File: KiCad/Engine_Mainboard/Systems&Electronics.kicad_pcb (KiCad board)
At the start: 2 copper layers, 182.4 x 143.2 mm, 54 parts, among them J1 Pressure Transducer, J12 Screw_Terminal_01x02, J13 Screw_Terminal_01x03, J2 Pressure Transducer, J3 Pressure Transducer, J4 Pressure Transducer, J5 Pressure Transducer, J6 Pressure Transducer

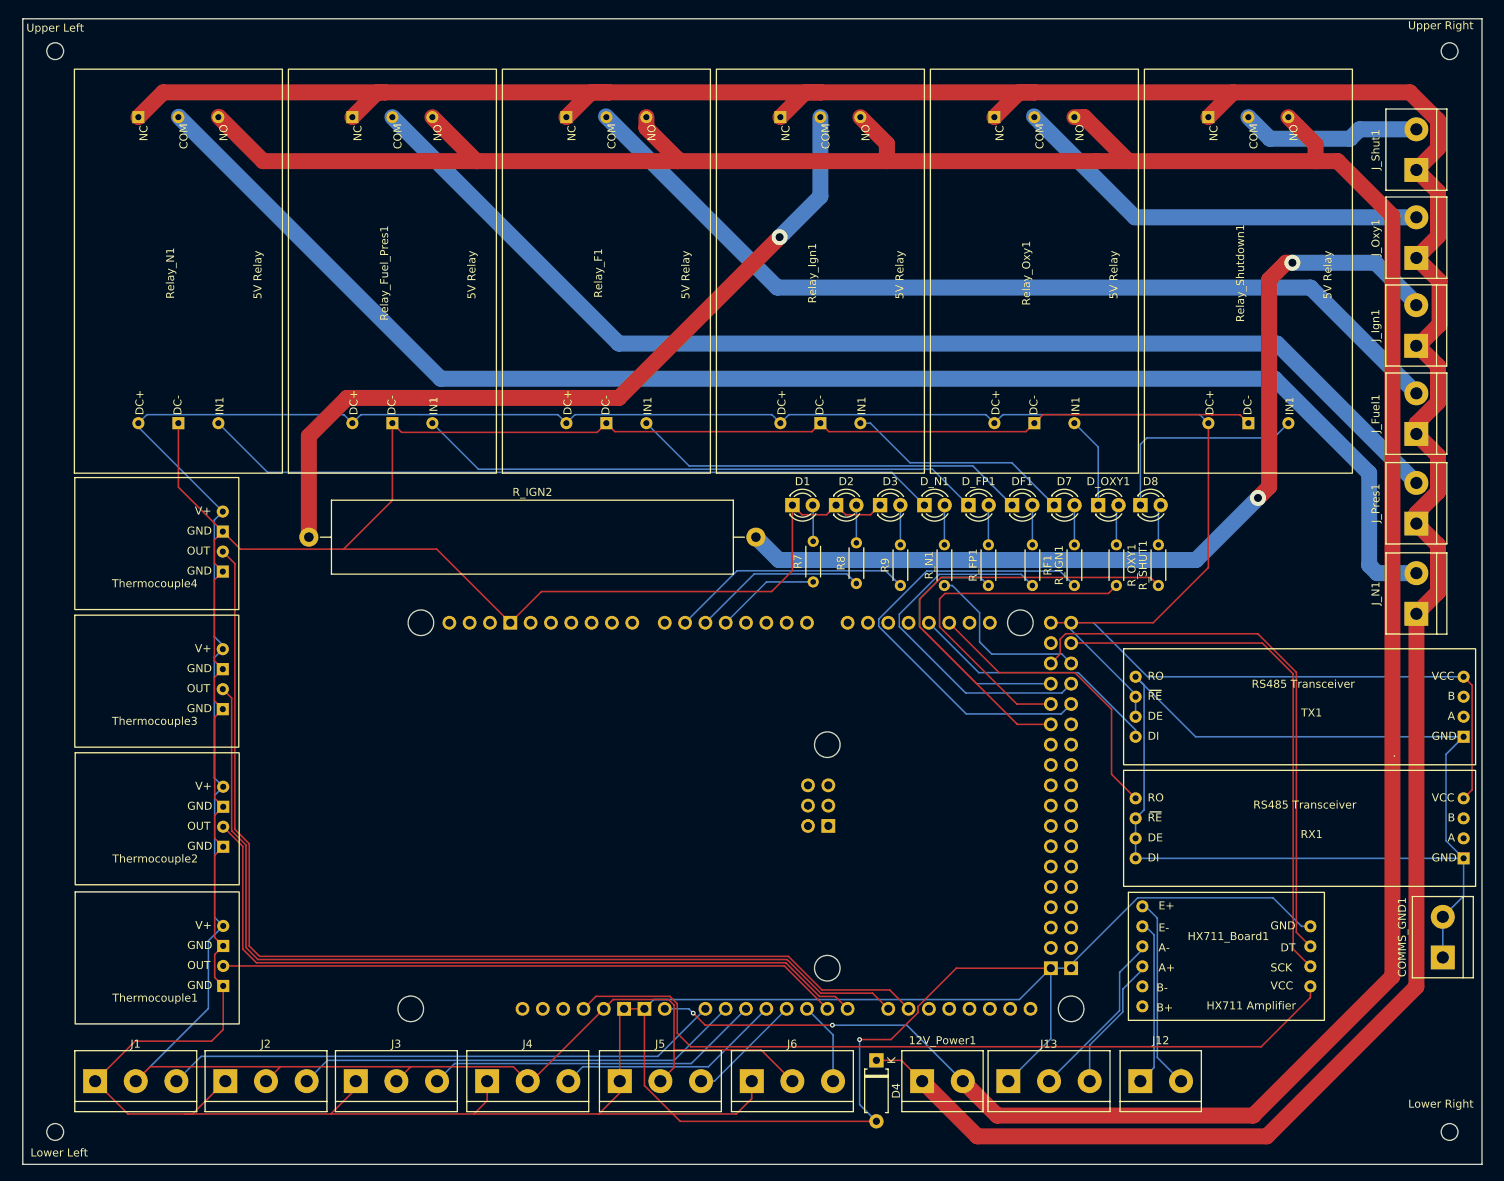
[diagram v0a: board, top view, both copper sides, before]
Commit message: PCB design reorg
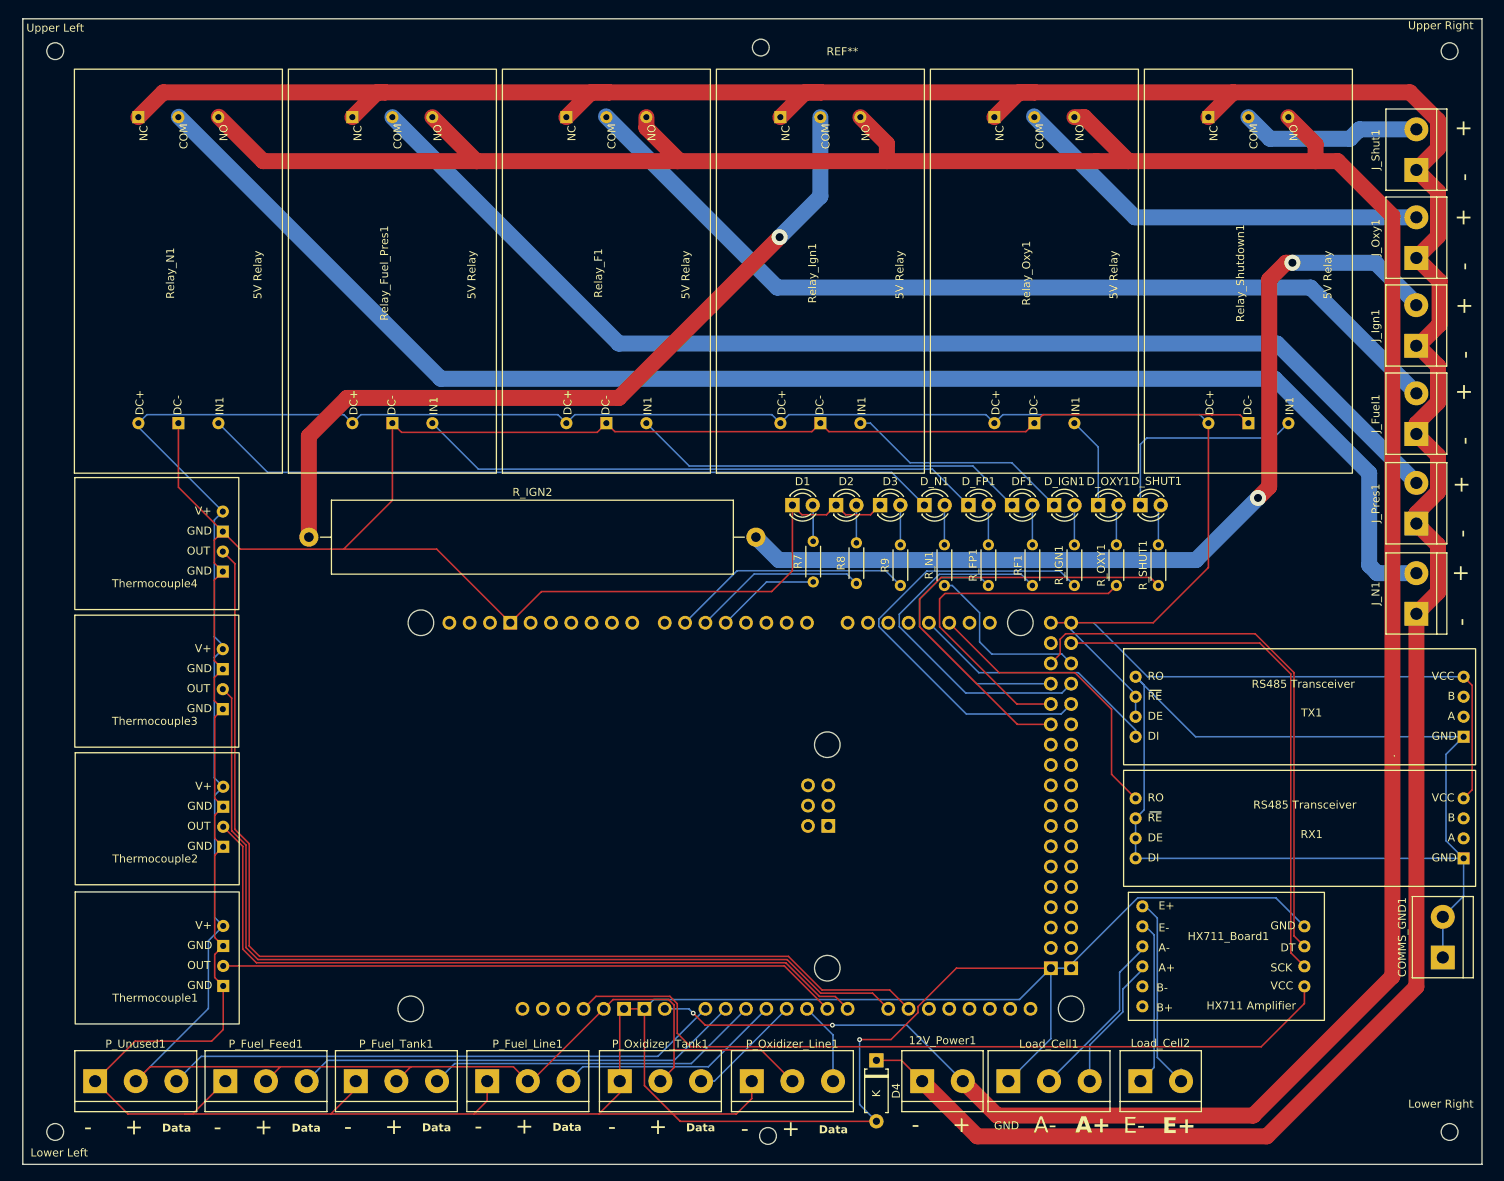
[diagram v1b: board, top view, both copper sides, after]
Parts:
- added REF**: MountingHole_2.1mm, MountingHole:MountingHole_2.1mm, F.Cu at (125.0, 23.8)
- added REF**: MountingHole_2.1mm, MountingHole:MountingHole_2.1mm, F.Cu at (126.0, 159.8)
- renumbered D7 to D_IGN1, D8 to D_SHUT1, J13 to Load_Cell1, J12 to Load_Cell2, J2 to P_Fuel_Feed1, J4 to P_Fuel_Line1, J3 to P_Fuel_Tank1, J6 to P_Oxidizer_Line1, J5 to P_Oxidizer_Tank1, J1 to P_Unused1
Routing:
- net Net-(D1-K): track 638.8 -> 637.6 mm
- net Net-(A1-PadD24): track 70.3 -> 69.8 mm
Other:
- board text added: "+"
- board text added: "-"
- board text added: "A+"
- board text added: "A-"
- board text added: "Data"
- board text added: "E+"
- board text added: "E-"
- board text added: "GND"
- board text added: "The edge holes are all the same size and spacing from the edge."
- board text removed: "The corner holes are all the same size and spacing from the edge."

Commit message: PCB Ignition Resistor Move
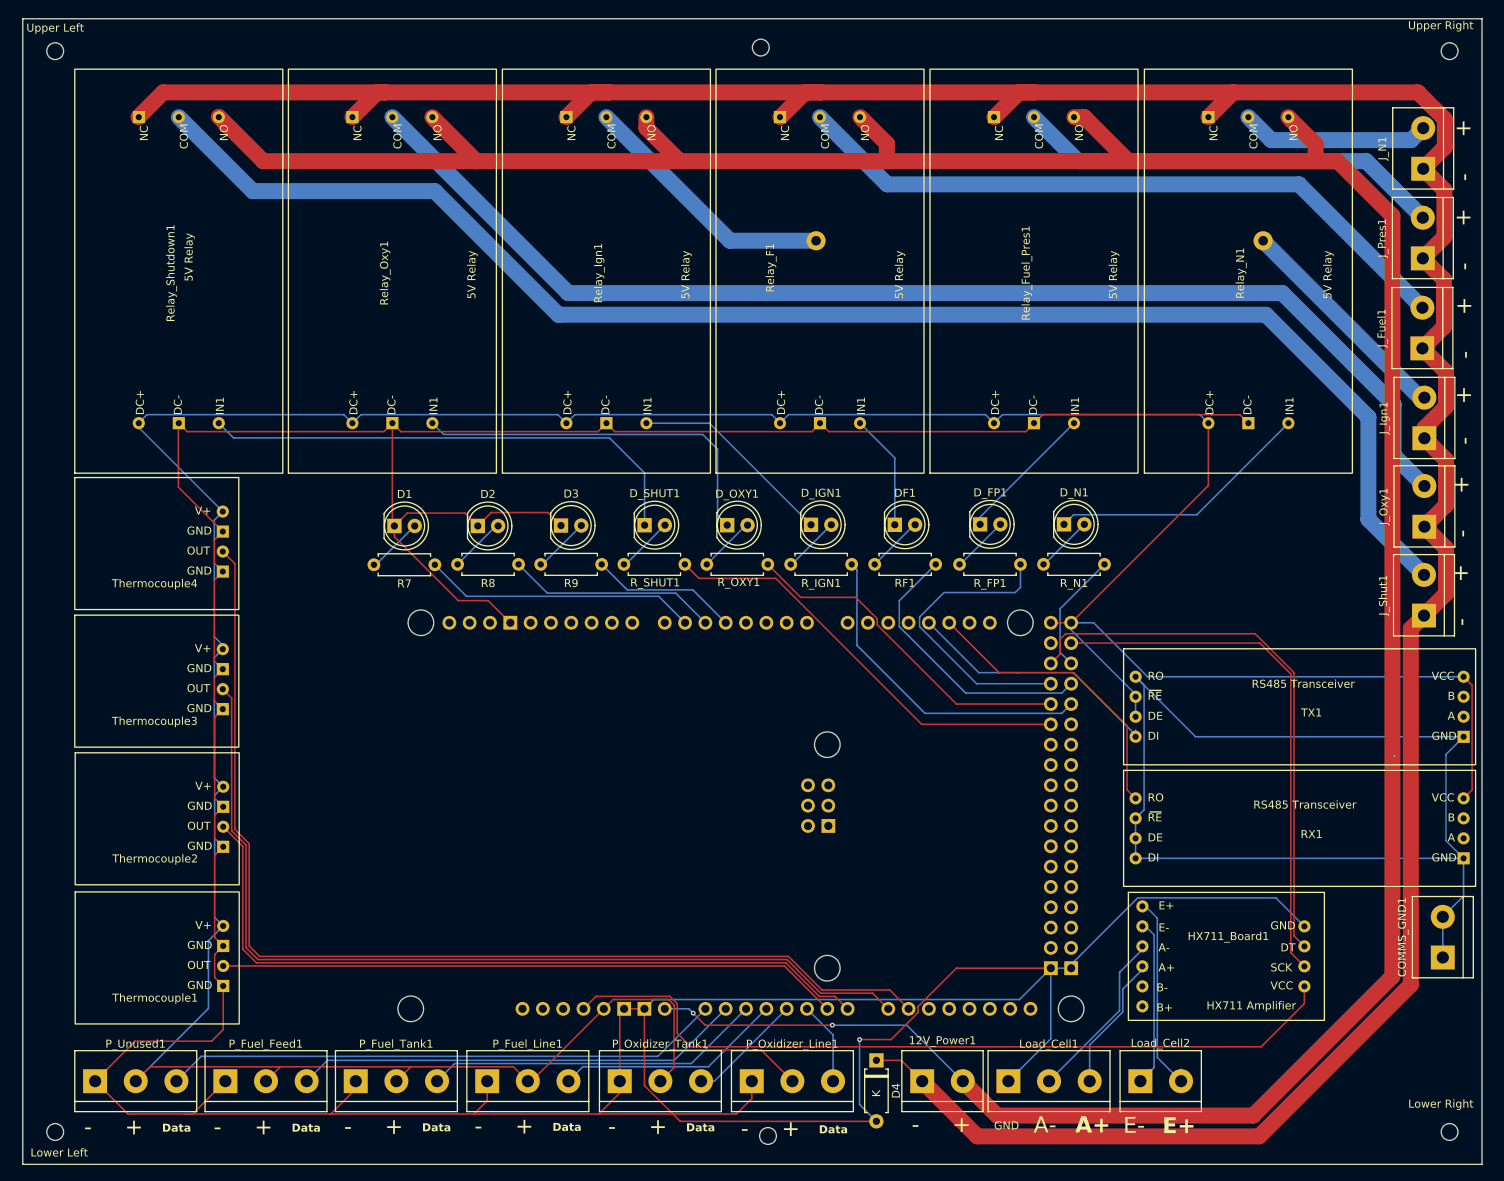
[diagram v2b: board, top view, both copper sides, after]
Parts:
- D1, D2, D3, DF1, D_FP1, D_IGN1, D_N1, D_OXY1, D_SHUT1: footprint LED_THT:LED_D3.0mm -> LED_THT:LED_D5.0mm
- R7, R8, R9, RF1, R_FP1, R_IGN1, R_N1, R_OXY1, R_SHUT1: footprint Resistor_THT:R_Axial_DIN0204_L3.6mm_D1.6mm_P5.08mm_Horizontal -> Resistor_THT:R_Axial_DIN0207_L6.3mm_D2.5mm_P7.62mm_Horizontal
- R_IGN2: moved to B.Cu
- moved Relay_N1 133.8 mm to (185.5, 52.0)
- moved Relay_Shutdown1 133.7 mm to (51.8, 52.0)
- moved Relay_Oxy1 80.2 mm to (78.5, 52.0)
- moved Relay_Fuel_Pres1 80.2 mm to (158.7, 52.0)
- moved R_IGN2 73.4 mm to (132.0, 48.0)
- moved D_SHUT1 62.0 mm to (110.5, 83.5)
- moved R_SHUT1 59.2 mm to (115.6, 88.4), turned to 180 degrees
- moved J_Shut1 55.7 mm to (207.9, 94.8)
- moved J_N1 55.6 mm to (207.8, 39.0)
- moved R_OXY1 51.3 mm to (118.3, 88.4), turned to 0 degrees
- moved D1 49.8 mm to (79.2, 83.6)
- moved R7 47.3 mm to (84.3, 88.5), turned to 180 degrees
- moved D_OXY1 46.4 mm to (120.8, 83.5)
- moved D2 44.9 mm to (89.7, 83.6)
- moved R8 42.3 mm to (94.8, 88.4), turned to 180 degrees
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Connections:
- R7 pad 1: Net-(A1-PadD4) -> Net-(A1-PadD6)
- R9 pad 1: Net-(A1-PadD6) -> Net-(A1-PadD4)
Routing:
- net Net-(J_Shut1-Pin_2): track 22.6 -> 186.8 mm
- net Net-(J_N1-Pin_2): track 185.1 -> 23.7 mm
- net Net-(J_Oxy1-Pin_2): track 53.0 -> 151.8 mm
- net Net-(J_Pres1-Pin_2): track 146.9 -> 53.8 mm
- net Net-(J_Ign1-Pin_2): track 116.7 -> 28.3 mm, vias 2 -> 0
- net Net-(R_IGN2-Pad1): track 98.9 -> 32.6 mm, vias 1 -> 0
- net Net-(D_N1-K): track 92.5 -> 33.3 mm
- net Net-(D_FP1-K): track 71.2 -> 17.5 mm
- net Net-(D_OXY1-K): track 11.5 -> 47.0 mm
- net Net-(DF1-K): track 50.0 -> 14.5 mm
- net Net-(D_SHUT1-K): track 27.2 -> 62.3 mm
- net Net-(D1-K): track 637.6 -> 603.8 mm
- net Net-(J_Fuel1-Pin_2): track 115.6 -> 85.2 mm
- net Net-(A1-PadD29): track 57.7 -> 41.2 mm
- net Net-(A1-PadD27): track 46.2 -> 35.1 mm
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
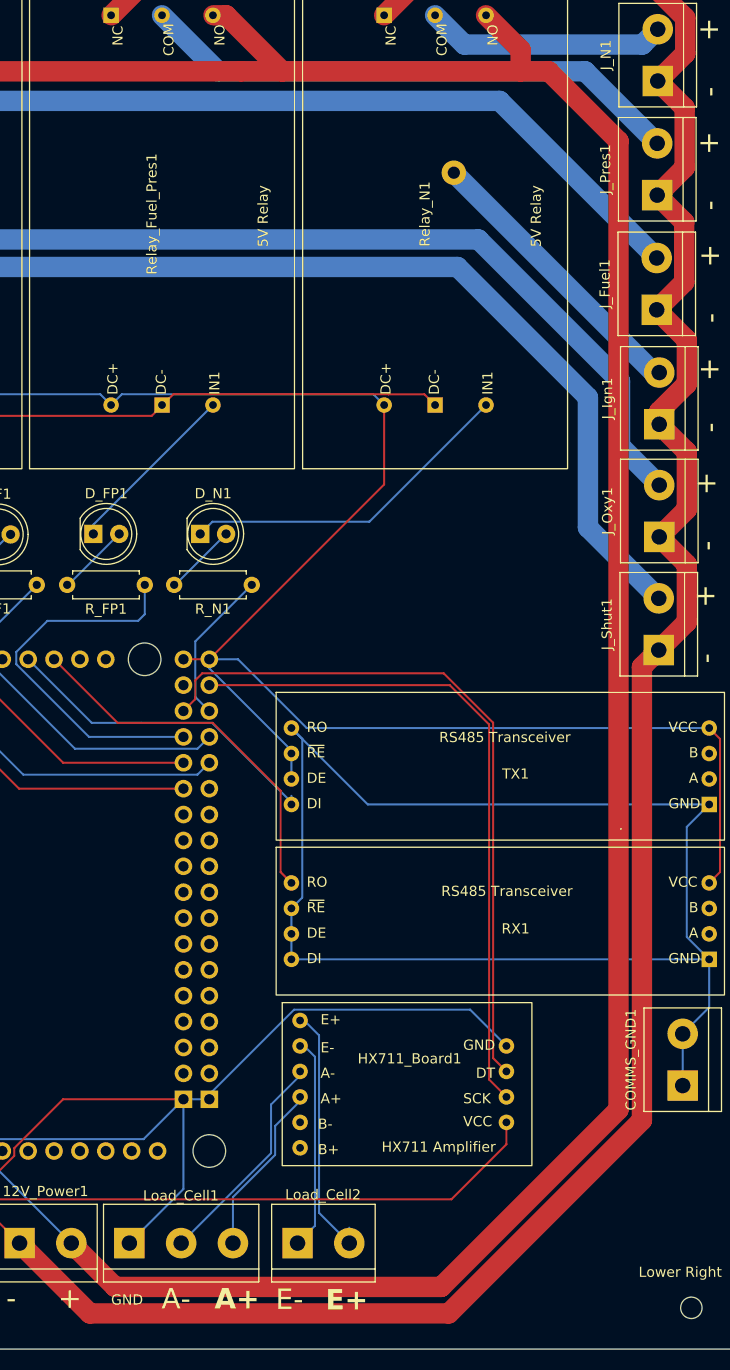
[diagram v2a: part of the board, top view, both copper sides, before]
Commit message: PCB minor trace move
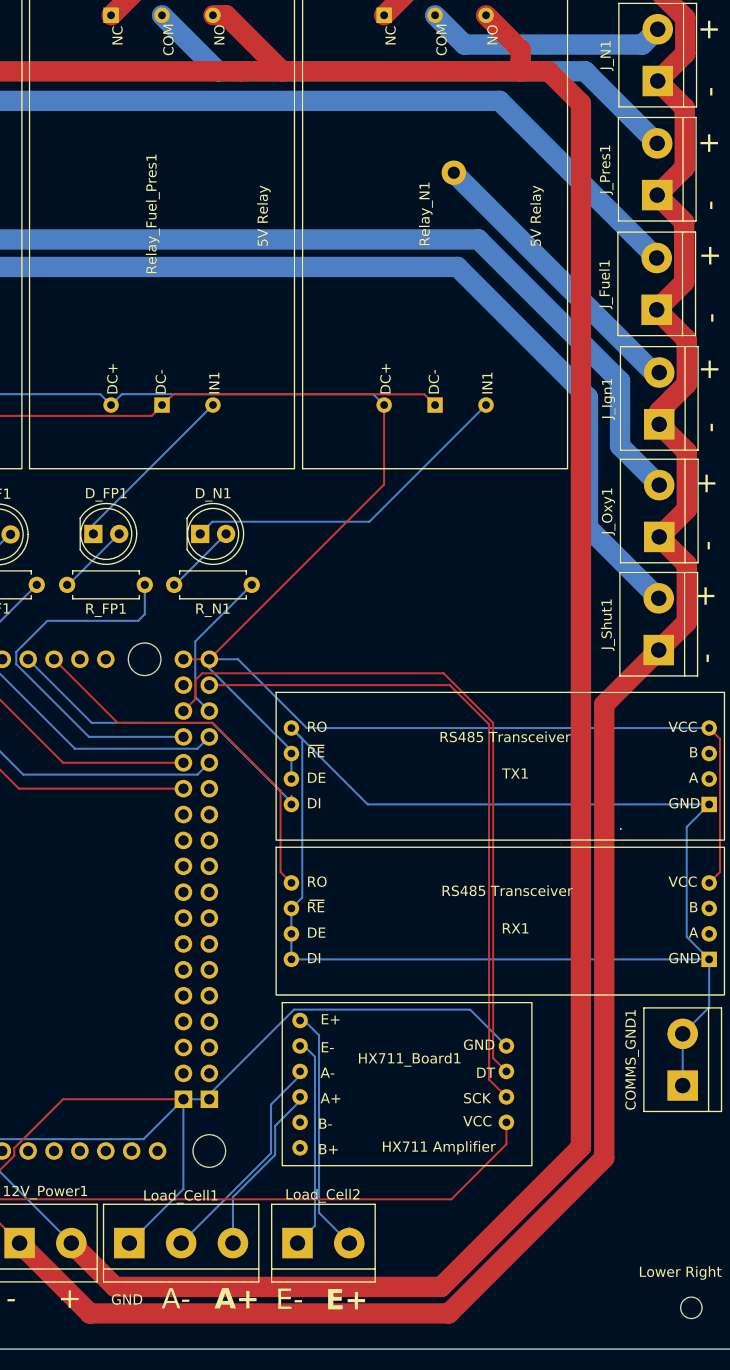
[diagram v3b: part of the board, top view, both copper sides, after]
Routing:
- net Net-(12V_Power1-Pin_2): track 388.4 -> 385.3 mm
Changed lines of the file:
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@@
+	)
+	(segment
+		(start 187.35 159.9)
+		(end 202.6 144.65)
+		(width 2)
+		(layer "F.Cu")
+		(net 1)
+	)
+	(segment
+		(start 145.22 153)
+		(end 152.12 159.9)
+		(width 2)
+		(layer "F.Cu")
+		(net 1)
 	)
 	(segment
@@
 	)
 	(segment
-		(start 187.35 159.9)
-		(end 206.3 140.95)
-		(width 2)
-		(layer "F.Cu")
-		(net 1)
-	)
-	(segment
 		(start 77.1 29.4)
 		(end 74 32.5)
@@
 	)
 	(segment
+		(start 210.7 86.39)
+		(end 208 83.69)
+		(width 2)
+		(layer "F.Cu")
+		(net 1)
+	)
+	(segment
+		(start 210.7 92.05)
+		(end 210.7 86.39)
+		(width 2)
+		(layer "F.Cu")
+		(net 1)
+	)
+	(segment
+		(start 210.55 32.751623)
+		(end 207.198377 29.4)
+		(width 2)
+		(layer "F.Cu")
+		(net 1)
+	)
+	(segment
+		(start 139.5 150.4)
+		(end 142.62 150.4)
+		(width 0.2)
+		(layer "F.Cu")
+		(net 1)
+	)
+	(segment
+		(start 157.35 29.4)
+		(end 154.25 32.5)
+		(width 2)
+		(layer "F.Cu")
+		(net 1)
+	)
+	(segment
+		(start 78.1 29.4)
+		(end 77.1 29.4)
+		(width 2)
+		(layer "F.Cu")
+		(net 1)
+	)
+	(segment
+		(start 50.35 29.4)
+		(end 47.25 32.5)
+		(width 2)
+		(layer "F.Cu")
+		(net 1)
+	)
+	(segment
+		(start 207.8 50.15)
+		(end 210.5 47.45)
+		(width 2)
+		(layer "F.Cu")
+		(net 1)
+	)
+	(segment
+		(start 202.6 100.15)
+		(end 207.95 94.8)
+		(width 2)
+		(layer "F.Cu")
+		(net 1)
+	)
+	(segment
+		(start 207.198377 29.4)
+		(end 184.1 29.4)
+		(width 2)
+		(layer "F.Cu")
+		(net 1)
+	)
+	(segment
 		(start 152.12 159.9)
 		(end 187.35 159.9)
@@
 	)
 	(segment
-		(start 210.7 86.39)
-		(end 208 83.69)
-		(width 2)
-		(layer "F.Cu")
-		(net 1)
-	)
-	(segment
-		(start 210.7 92.05)
-		(end 210.7 86.39)
-		(width 2)
-		(layer "F.Cu")
-		(net 1)
-	)
-	(segment
-		(start 210.55 32.751623)
-		(end 207.198377 29.4)
-		(width 2)
-		(layer "F.Cu")
-		(net 1)
-	)
-	(segment
-		(start 139.5 150.4)
-		(end 142.62 150.4)
-		(width 0.2)
-		(layer "F.Cu")
-		(net 1)
-	)
-	(segment
-		(start 157.35 29.4)
-		(end 154.25 32.5)
-		(width 2)
-		(layer "F.Cu")
-		(net 1)
-	)
-	(segment
-		(start 78.1 29.4)
-		(end 77.1 29.4)
-		(width 2)
-		(layer "F.Cu")
-		(net 1)
-	)
-	(segment
-		(start 50.35 29.4)
-		(end 47.25 32.5)
-		(width 2)
-		(layer "F.Cu")
-		(net 1)
-	)
-	(segment
-		(start 207.8 50.15)
-		(end 210.5 47.45)
-		(width 2)
-		(layer "F.Cu")
-		(net 1)
-	)
-	(segment
-		(start 207.198377 29.4)
-		(end 184.1 29.4)
-		(width 2)
-		(layer "F.Cu")
-		(net 1)
-	)
-	(segment
 		(start 207.85 38.95)
 		(end 210.55 36.25)
@@
 	)
 	(segment
-		(start 206.3 140.95)
-		(end 206.3 96.45)
-		(width 2)
-		(layer "F.Cu")
-		(net 1)
-	)
-	(segment
 		(start 103.85 29.4)
 		(end 100.75 32.5)
@@
 	)
 	(segment
-		(start 145.22 153)
-		(end 152.12 159.9)
-		(width 2)
-		(layer "F.Cu")
-		(net 1)
-	)
-	(segment
-		(start 206.3 96.45)
-		(end 207.95 94.8)
-		(width 2)
-		(layer "F.Cu")
-		(net 1)
-	)
-	(segment
 		(start 210.55 36.25)
 		(end 210.55 32.751623)
@@
 	)
 	(segment
+		(start 202.6 144.65)
+		(end 202.6 100.15)
+		(width 2)
+		(layer "F.Cu")
+		(net 1)
+	)
+	(segment
 		(start 184.1 29.4)
 		(end 181 32.5)
@@
 	)
 	(segment
+		(start 150.3 153)
+		(end 154.6 157.3)
+		(width 2)
+		(layer "F.Cu")
+		(net 111)
+	)
+	(segment
 		(start 110.75 33.85)
 		(end 114.662 37.762)
@@
 	)
 	(segment
+		(start 197.162 38)
+		(end 194.4 38)
+		(width 2)
+		(layer "F.Cu")
+		(net 111)
+	)
+	(segment
 		(start 165.5 32.5)
 		(end 164.25 32.5)
@@
 	)
 	(segment
-		(start 186.6 157.3)
-		(end 154.6 157.3)
-		(width 2)
-		(layer "F.Cu")
-		(net 111)
-	)
-	(segment
-		(start 204 44.838)
-		(end 197.162 38)
-		(width 2)
-		(layer "F.Cu")
-		(net 111)
-	)
-	(segment
 		(start 171 38)
 		(end 165.5 32.5)
@@
 	)
 	(segment
-		(start 186.6 157.3)
-		(end 204 139.9)
-		(width 2)
-		(layer "F.Cu")
-		(net 111)
-	)
-	(segment
 		(start 89.6 38)
 		(end 62.85 38)
@@
 	)
 	(segment
-		(start 154.6 157.3)
-		(end 150.3 153)
-		(width 2)
-		(layer "F.Cu")
-		(net 111)
-	)
-	(segment
 		(start 110.75 32.5)
 		(end 110.75 33.85)
@@
 	)
 	(segment
-		(start 204 139.9)
-		(end 204 44.838)
-		(width 2)
-		(layer "F.Cu")
-		(net 111)
-	)
-	(segment
 		(start 140.812 35.812)
 		(end 140.812 38)
@@
 	)
 	(segment
-		(start 197.162 38)
-		(end 194.4 38)
+		(start 200.31 143.59)
+		(end 200.31 41.148)
+		(width 2)
+		(layer "F.Cu")
+		(net 111)
+	)
+	(segment
+		(start 154.6 157.3)
+		(end 186.6 157.3)
 		(width 2)
 		(layer "F.Cu")
@@
 		(layer "F.Cu")
 		(net 111)
+	)
+	(segment
+		(start 200.31 41.148)
+		(end 197.162 38)
+		(width 2)
+		(layer "F.Cu")
+		(net 111)
+	)
+	(segment
+		(start 186.6 157.3)
+		(end 200.31 143.59)
+		(width 2)
+		(layer "F.Cu")
+		(net 111)
